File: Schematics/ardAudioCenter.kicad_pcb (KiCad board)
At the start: 2 copper layers, 1 part, among them U1 Arduino_Mini_Pro

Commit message: pcb
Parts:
- added A1: Arduino_Nano_v3.x, My_Arduino:Arduino_Nano_WithMountingHoles_larger, F.Cu at (116.8, 76.2)
- added C1: 0.47u, My_Misc:CP_Radial_D5.0mm_P2.50mm_larger_pads, F.Cu at (160.8, 111.9)
- added C2: 0.47u, My_Misc:CP_Radial_D5.0mm_P2.50mm_larger_pads, F.Cu at (186.9, 86.5)
- added C3: 0.47u, My_Misc:CP_Radial_D5.0mm_P2.50mm_larger_pads, F.Cu at (168.8, 100.2)
- added C4: 0.47u, My_Misc:CP_Radial_D5.0mm_P2.50mm_larger_pads, F.Cu at (154.2, 111.9)
- added C5: 0.33u, My_Misc:CP_Radial_D5.0mm_P2.00mm_larger, F.Cu at (171.6, 93.1)
- added C6: 0.1u, My_Misc:CP_Radial_D5.0mm_P2.00mm_larger, F.Cu at (147.8, 110.9)
- added J1: 4-pin_I2C_LCD_header, My_Headers:4-pin_I2C_LCD_header_larger, F.Cu at (170.8, 73.9)
- added R1: 10k, My_Misc:R_Axial_DIN0207_L6.3mm_D2.5mm_P10.16mm_Horizontal_larger_pads, F.Cu at (157.1, 94.9)
- added R2: 10k, My_Misc:R_Axial_DIN0207_L6.3mm_D2.5mm_P10.16mm_Horizontal_larger_pads, F.Cu at (136.1, 116.8)
- added U10: 4-pole_RL-input_screw_terminal, My_Parts:4-pole_screw_terminal_RL_input, F.Cu at (163.0, 74.8)
- added U11: 4-pole_RL-input_screw_terminal, My_Parts:4-pole_screw_terminal_RL_input, F.Cu at (151.7, 74.8)
- added U14: L7805, My_Misc:TO-220-3_Vertical_larger, F.Cu at (171.7, 87.8)
- added U15: 2-pole_power_in_screw_terminal, My_Parts:2-pole_power_in_screw_terminal, F.Cu at (190.7, 74.8)
- added U3: KY-040_Rotary_Encoder, My_Headers:5-pin_KY-040_rotary_encoder_header_larger, F.Cu at (152.8, 95.2)
- added U5: 4-pole_RL-output_screw_terminal, My_Parts:4-pole_screw_terminal_RL_output, F.Cu at (140.0, 96.7)
- added U6: MCP41010, My_Misc:DIP-8_W7.62mm_large, F.Cu at (157.1, 99.0)
- added U7: CD4052B, My_Misc:DIP-16_W7.62mm_larger, F.Cu at (136.1, 73.7)
- added U8: MCP41010, My_Misc:DIP-8_W7.62mm_large, F.Cu at (175.1, 73.7)
- U1: value Arduino_Mini_Pro -> KY-040_Rotary_Encoder; footprint My_Arduino:Arduino_Pro_Mini_vC_larger_pads -> My_Headers:5-pin_KY-040_rotary_encoder_header_larger
- moved U1 41.6 mm to (148.1, 95.2)
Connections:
- U1 pad 4: Net-(U1-Pad4) -> +5V
- U1 pad 5: Net-(U1-Pad5) -> GND

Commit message: pcb routing
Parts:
- added U16: TEA5767_FM_Radio_Module, My_Headers:4-pin_TEA5767_radio_module_header_large, F.Cu at (94.6, 62.9)
- added U17: 3-pin_potentiometer_output, My_Headers:3-pin_potentiometer_header_larger_pads, F.Cu at (202.6, 70.5)
- added U9: 3-pin_potentiometer_output, My_Headers:3-pin_potentiometer_header_larger_pads, F.Cu at (177.8, 70.5)
- C1: renamed from C5; footprint My_Misc:CP_Radial_D5.0mm_P2.00mm_larger -> My_Misc:C_Disc_D7.5mm_W2.5mm_P5.00mm_larger
- C2: renamed from C1; footprint My_Misc:CP_Radial_D5.0mm_P2.50mm_larger_pads -> My_Misc:C_Disc_D7.5mm_W2.5mm_P5.00mm_larger
- C3: renamed from C2; footprint My_Misc:CP_Radial_D5.0mm_P2.50mm_larger_pads -> My_Misc:C_Disc_D7.5mm_W2.5mm_P5.00mm_larger
- C4: renamed from C6; footprint My_Misc:CP_Radial_D5.0mm_P2.00mm_larger -> My_Misc:C_Disc_D7.5mm_W2.5mm_P5.00mm_larger
- C5: renamed from C3; footprint My_Misc:CP_Radial_D5.0mm_P2.50mm_larger_pads -> My_Misc:C_Disc_D7.5mm_W2.5mm_P5.00mm_larger
- C6: renamed from C4; footprint My_Misc:CP_Radial_D5.0mm_P2.50mm_larger_pads -> My_Misc:C_Disc_D7.5mm_W2.5mm_P5.00mm_larger
- moved U1 128.6 mm to (62.2, 67.3)
- moved C1 103.2 mm to (71.8, 67.3)
- moved U3 90.2 mm to (83.8, 67.3), turned to 270 degrees
- moved C4 81.3 mm to (76.2, 72.4), turned to 180 degrees
- moved U7 79.7 mm to (62.2, 79.4)
- moved J1 76.2 mm to (94.6, 73.7), turned to 90 degrees
- moved C5 69.4 mm to (101.0, 85.7), turned to 270 degrees
- moved C6 52.1 mm to (109.2, 85.7), turned to 270 degrees
- moved U14 51.7 mm to (199.4, 94.6), turned to 180 degrees
- moved U10 46.0 mm to (92.1, 87.0), turned to 270 degrees
- moved C3 42.8 mm to (144.1, 85.7), turned to 270 degrees
- moved U8 36.3 mm to (161.3, 62.9)
- moved C2 36.2 mm to (135.9, 85.7), turned to 270 degrees
- moved U5 28.6 mm to (125.7, 85.7), turned to 270 degrees
- moved R2 22.2 mm to (125.7, 97.2), turned to 180 degrees
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- renumbered U15 to U1, U7 to U10, U8 to U11, U10 to U13, U11 to U14, U1 to U2, U14 to U3, U3 to U5, U5 to U7, U6 to U8
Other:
- net class Default: clearance 0.2 -> 0.508; trace_width 0.25 -> 0.762; via_dia 0.8 -> 3.048; via_drill 0.4 -> 0.762
- rule trace_clearance: 0.2 -> 0.508

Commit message: pcb v1
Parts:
- added REF**: MountingHole_3.2mm_M3, MountingHole:MountingHole_3.2mm_M3, F.Cu at (90.8, 98.4)
- added REF**: MountingHole_3.2mm_M3, MountingHole:MountingHole_3.2mm_M3, F.Cu at (175.3, 98.4)
- added REF**: MountingHole_3.2mm_M3, MountingHole:MountingHole_3.2mm_M3, F.Cu at (175.3, 47.6)
- added REF**: MountingHole_3.2mm_M3, MountingHole:MountingHole_3.2mm_M3, F.Cu at (73.7, 47.6)
- moved U17 82.2 mm to (123.8, 47.0), turned to 0 degrees
- moved U11 47.7 mm to (139.1, 54.6), turned to 180 degrees
- moved U9 38.5 mm to (147.3, 47.0), turned to 0 degrees
- moved U14 35.9 mm to (173.4, 69.8)
- moved C4 30.5 mm to (97.2, 50.2)
- moved U1 24.2 mm to (83.2, 55.2), turned to 180 degrees
- moved C1 23.7 mm to (92.2, 55.2)
- moved U3 23.6 mm to (104.1, 55.2), turned to 90 degrees
- moved J1 21.1 mm to (73.7, 76.2)
- moved U16 21.1 mm to (73.7, 65.4)
- moved R1 15.9 mm to (146.1, 92.7), turned to 0 degrees
- moved U7 15.5 mm to (76.8, 84.5)
- moved U2 15.4 mm to (146.1, 87.6), turned to 90 degrees
- moved C6 8.57 mm to (114.3, 92.6), turned to 90 degrees
- moved C5 8.47 mm to (109.2, 87.6)
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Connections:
- C5 pad 1: Net-(A1-Pad6) -> Net-(A1-Pad5)
- C6 pad 2: Net-(A1-Pad5) -> Net-(A1-Pad6)
- U13 pad 2: Net-(U13-Pad2) -> GND
- U5 pad 1: Net-(A1-Pad6) -> Net-(A1-Pad5)
- U5 pad 2: Net-(A1-Pad5) -> Net-(A1-Pad6)
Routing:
- net GND: track 0.00 -> 382.4 mm, vias 0 -> 3
- net +5V: track 0.00 -> 296.4 mm, vias 0 -> 10
- net LineL+: track 0.00 -> 111.6 mm, vias 0 -> 2
- net LineR+: track 0.00 -> 105.8 mm, vias 0 -> 2
- net BTR+: track 0.00 -> 96.0 mm
- net BTL+: track 0.00 -> 81.1 mm, vias 0 -> 2
- net Net-(A1-Pad23): track 0.00 -> 73.9 mm
- net Net-(A1-Pad14): track 0.00 -> 71.8 mm
- net Net-(A1-Pad24): track 0.00 -> 62.6 mm
- net Net-(A1-Pad19): track 0.00 -> 60.7 mm
- net Net-(A1-Pad20): track 0.00 -> 55.3 mm
- net Net-(A1-Pad16): track 0.00 -> 55.2 mm
- net Net-(A1-Pad9): track 0.00 -> 31.9 mm
- net Net-(A1-Pad21): track 0.00 -> 30.5 mm
- net Net-(A1-Pad10): track 0.00 -> 29.4 mm
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- added copper zone on B.Cu, net (none)
- added copper zone on B.Cu, net GND
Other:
- board outline added: 109.2 x 58.4 mm
- board text added: "ardAudioCenter Design: Jon Sagebrand jonsagebrand@gmail.com"

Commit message: PCB v1.1
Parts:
- added J1: 2-pin_power_input_header, My_Headers:2-pin_power_input_header, F.Cu at (116.2, 54.6)
- renumbered J1 to J3
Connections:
- net Net-(U10-Pad13) renamed /Rout+
- net Net-(U10-Pad3) renamed /Lout+
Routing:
- net +5V: track 296.4 -> 301.8 mm
- net FMR+: track 0.00 -> 5.08 mm, vias 0 -> 1
- net FML+: track 0.00 -> 4.86 mm, vias 0 -> 1
- net GND: track 382.4 -> 387.2 mm
- net LineL+: track 111.6 -> 113.9 mm

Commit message: schematics
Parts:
- removed REF** (x4): MountingHole_3.2mm_M3, MountingHole:MountingHole_3.2mm_M3
- J1: footprint My_Headers:2-pin_power_input_header -> My_Headers:2-pin_power_input_header_larger_pads

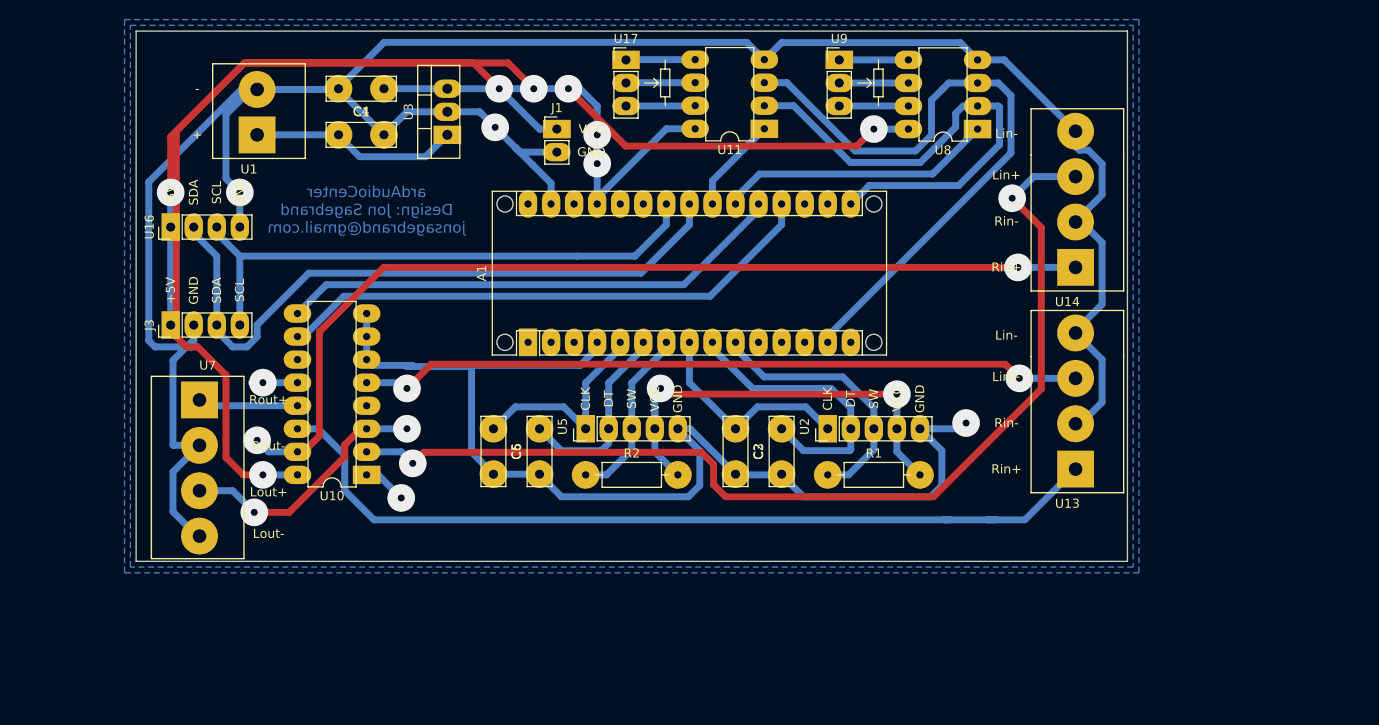
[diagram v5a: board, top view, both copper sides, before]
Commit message: changed bt hookup
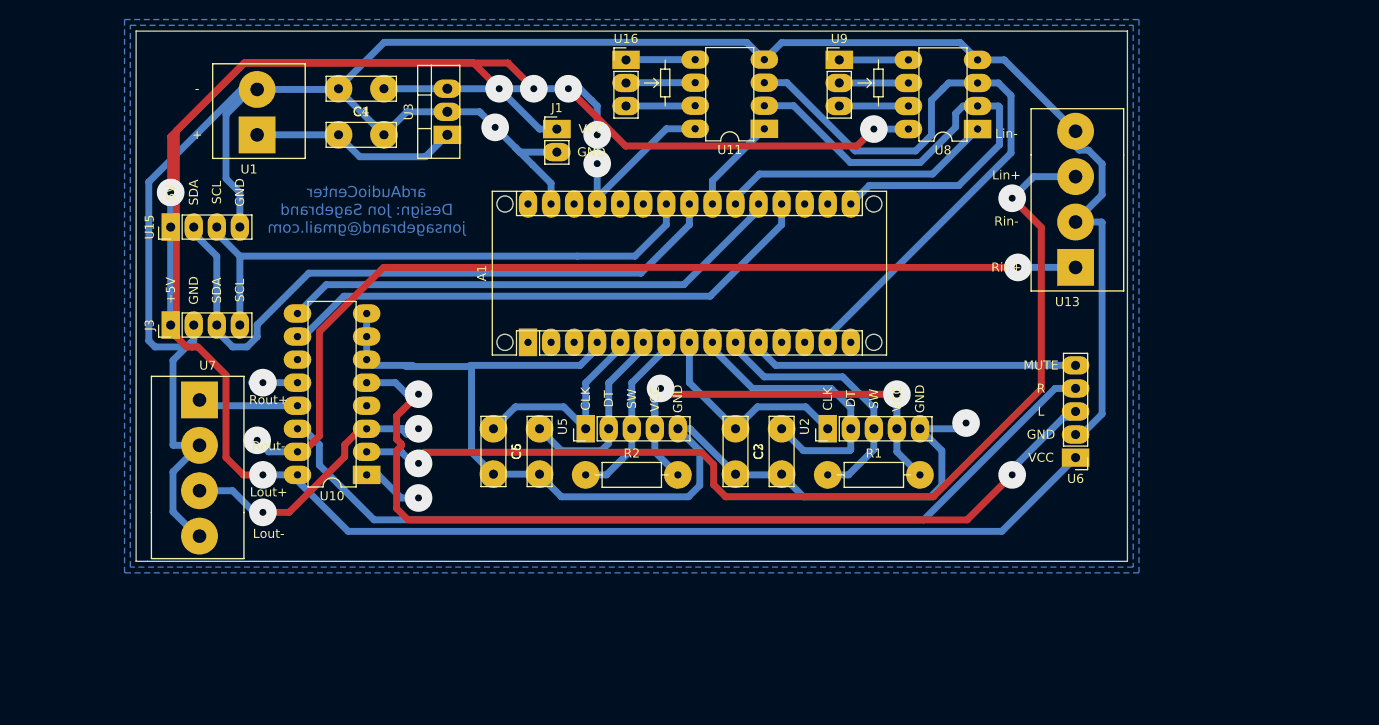
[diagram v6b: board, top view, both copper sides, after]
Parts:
- removed the U13 at (173.4, 92.1)
- added U6: JDY-62_Bluetooth_Module, My_Headers:5-pin_JDY-62_bluetooth_module_header_large, F.Cu at (173.4, 90.8)
- renumbered U14 to U13, U16 to U15, U17 to U16
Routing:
- net +5V: track 301.8 -> 393.2 mm
- net Net-(A1-Pad11): track 0.00 -> 36.4 mm
- net BTL+: track 81.0 -> 100.9 mm
- net FML+: track 4.86 -> 6.77 mm
- net /Lout+: track 29.1 -> 31.1 mm
- net BTR+: track 96.0 -> 97.2 mm
- net LineL+: track 113.9 -> 114.6 mm
- net GND: track 387.2 -> 387.3 mm, vias 3 -> 2

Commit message: new pcb
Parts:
- J1: footprint My_Headers:2-pin_power_input_header_larger_pads -> My_Headers:2-pin_power_input_header
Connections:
- A1 pad 1: Net-(A1-Pad1) -> unconnected-(A1-Pad1)
- A1 pad 15: Net-(A1-Pad15) -> unconnected-(A1-Pad15)
- A1 pad 17: Net-(A1-Pad17) -> unconnected-(A1-Pad17)
- A1 pad 18: Net-(A1-Pad18) -> unconnected-(A1-Pad18)
- A1 pad 2: Net-(A1-Pad2) -> unconnected-(A1-Pad2)
- A1 pad 25: Net-(A1-Pad25) -> unconnected-(A1-Pad25)
- A1 pad 26: Net-(A1-Pad26) -> unconnected-(A1-Pad26)
- A1 pad 28: Net-(A1-Pad28) -> unconnected-(A1-Pad28)
- A1 pad 3: Net-(A1-Pad3) -> unconnected-(A1-Pad3)
- A1 pad 30: Net-(A1-Pad30) -> unconnected-(A1-Pad30)
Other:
- net class Default removed
